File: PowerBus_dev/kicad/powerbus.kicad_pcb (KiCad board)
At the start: 2 copper layers, 1 part, among them Q1 XT60_YELLOW

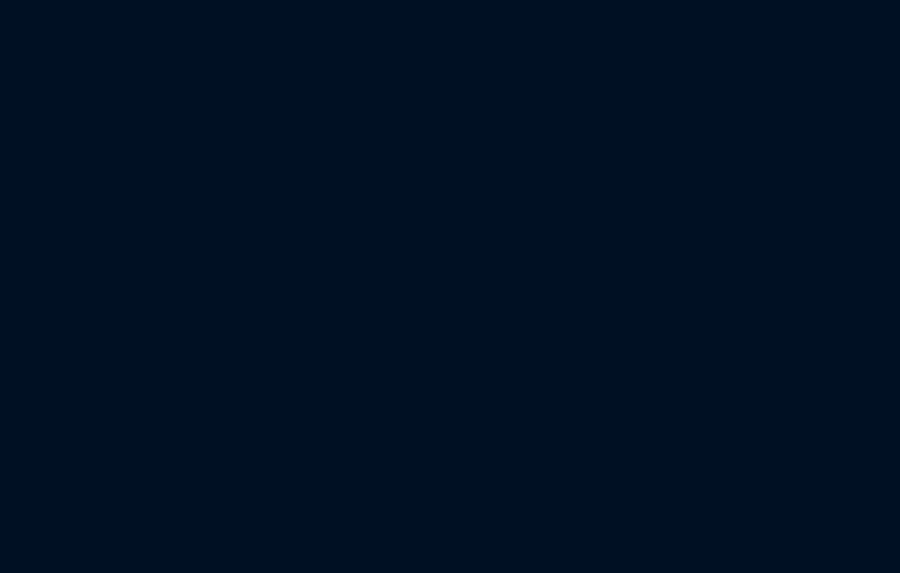
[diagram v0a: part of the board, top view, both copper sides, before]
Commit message: made basic power bus sch and pcb and made it into a 4 layer board
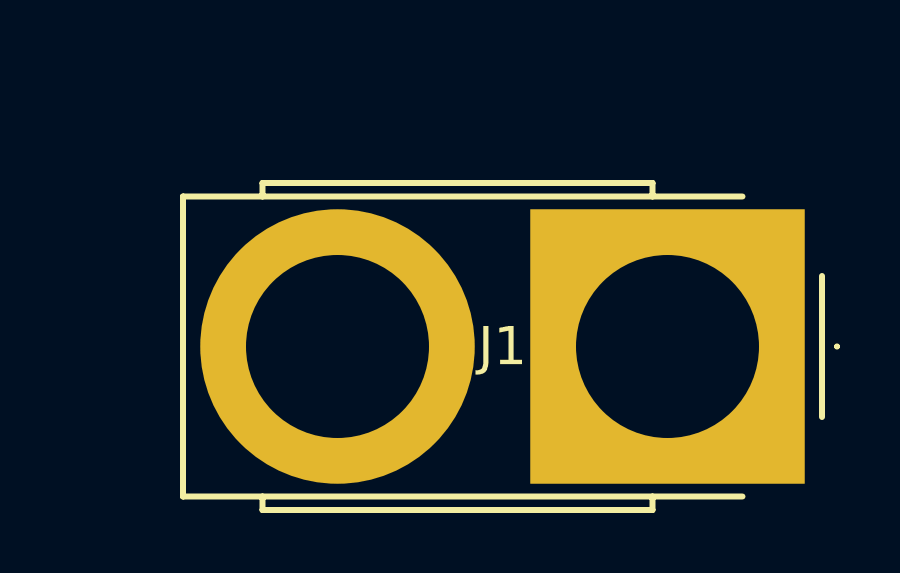
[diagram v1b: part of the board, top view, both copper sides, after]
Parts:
- added J1: XT90PB-F, powerbus lib:XT90PBF, F.Cu at (175.0, 92.0)

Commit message: changes to pcb
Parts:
- added Q2: XT60_YELLOW, powerbus lib:AMASS_XT60PB-M, F.Cu at (131.0, 75.0)
- added Q3: XT60_YELLOW, powerbus lib:AMASS_XT60PB-M, F.Cu at (142.0, 75.0)
- moved J1 73.8 mm to (105.0, 68.5), turned to 90 degrees
- moved Q1 12.8 mm to (120.0, 75.0), turned to -90 degrees
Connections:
- J1 pad 1: unconnected-(J1-Pad1) -> /GND
- J1 pad 2: unconnected-(J1-Pad2) -> /VCC
- Q1 pad 1: unconnected-(Q1-Pad1) -> /GND
- Q1 pad 2: unconnected-(Q1-Pad2) -> /VCC
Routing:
- added copper zone on In1.Cu, net /GND
- added copper zone on In2.Cu, net /VCC
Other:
- board outline added: 51 x 26 mm
- copper layers 2 -> 4
